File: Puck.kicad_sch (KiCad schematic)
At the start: 5 parts, among them SW1 SW_Push, SW2 SW_Push, U2 ESP32-C6-MINI-1/U

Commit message: feat: Disconnect RX and TX pins
Original-author: Ishan Karmakar <ishan.karmakar24@gmail.com>
Source-commit: 296c2ee0a068d96963a51e7bc8ff53979a0f6f0b
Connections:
- net RX: no longer names the net of U2.30 (U0RXD/GPIO17)
- net TX: no longer names the net of U2.31 (U0TXD/GPIO16)
- no-connect marks 12 -> 14
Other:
- sheet ExternalAutoprogramming (Low-Profile Female) ports: added none; removed RX, TX
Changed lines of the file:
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@@
+	)
+	(no_connect
+		(at 177.8 29.21)
 	)
 	(no_connect
@@
 	(no_connect
 		(at 121.92 57.15)
+	)
+	(no_connect
+		(at 177.8 31.75)
 	)
 	(wire
@@
 			(width 0)
 			(type default)
-		)
-	)
-	(label "TX"
-		(at 177.8 29.21 0)
-		(effects
-			(font
-				(size 1.27 1.27)
-			)
-			(justify left bottom)
 		)
 	)
@@
 		)
 	)
-	(label "RX"
-		(at 177.8 31.75 0)
-		(effects
-			(font
-				(size 1.27 1.27)
-			)
-			(justify left bottom)
-		)
-	)
 	(label "IO3"
 		(at 121.92 41.91 180)
@@
 		)
 	)
-	(label "RX"
-		(at 46.99 77.47 0)
-		(effects
-			(font
-				(size 1.27 1.27)
-			)
-			(justify left bottom)
-		)
-	)
 	(label "BOOT"
 		(at 29.21 77.47 180)
@@
 			)
 			(justify right bottom)
-		)
-	)
-	(label "TX"
-		(at 46.99 80.01 0)
-		(effects
-			(font
-				(size 1.27 1.27)
-			)
-			(justify left bottom)
 		)
 	)
@@
 			)
 		)
-		(pin "RX" bidirectional
-			(at 46.99 77.47 0)
-			(effects
-				(font
-					(size 1.27 1.27)
-				)
-				(justify right)
-			)
-		)
-		(pin "TX" bidirectional
-			(at 46.99 80.01 0)
-			(effects
-				(font
-					(size 1.27 1.27)
-				)
-				(justify right)
-			)
-		)

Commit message: feat: Remove the BOOT pin + NC GPIO9
Original-author: Ishan Karmakar <ishan.karmakar24@gmail.com>
Source-commit: 8bb5acb199ee9e43bb7b500971a5340ad49e3dfa
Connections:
- net BOOT: no longer names the net of U2.29 (GPIO23)
- net IO9: no longer names the net of U2.23 (GPIO9)
- no-connect marks 14 -> 16
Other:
- sheet ExternalAutoprogramming (Low-Profile Female) ports: added none; removed BOOT
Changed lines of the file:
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@@
+	)
+	(no_connect
+		(at 177.8 52.07)
 	)
 	(no_connect
@@
 	(no_connect
 		(at 177.8 29.21)
+	)
+	(no_connect
+		(at 177.8 72.39)
 	)
 	(no_connect
@@
 		)
 	)
-	(label "BOOT"
-		(at 177.8 72.39 0)
-		(effects
-			(font
-				(size 1.27 1.27)
-			)
-			(justify left bottom)
-		)
-	)
 	(label "IO3"
 		(at 121.92 41.91 180)
-		(effects
-			(font
-				(size 1.27 1.27)
-			)
-			(justify right bottom)
-		)
-	)
-	(label "IO9"
-		(at 177.8 52.07 0)
-		(effects
-			(font
-				(size 1.27 1.27)
-			)
-			(justify left bottom)
-		)
-	)
-	(label "BOOT"
-		(at 29.21 77.47 180)
 		(effects
 			(font
@@
 			)
 		)
-		(pin "BOOT" bidirectional
-			(at 29.21 77.47 180)
-			(effects
-				(font
-					(size 1.27 1.27)
-				)
-				(justify left)
-			)
-		)

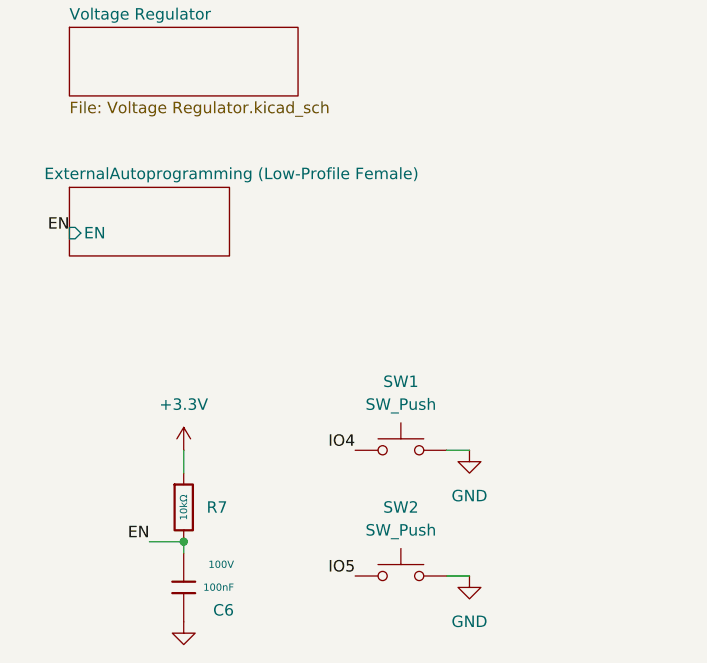
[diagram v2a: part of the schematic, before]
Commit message: feat: Remove autoprogramming sheet
Original-author: Ishan Karmakar <ishan.karmakar24@gmail.com>
Source-commit: 11d90a359a53dbe271e216bf89b8d8400085b4c9
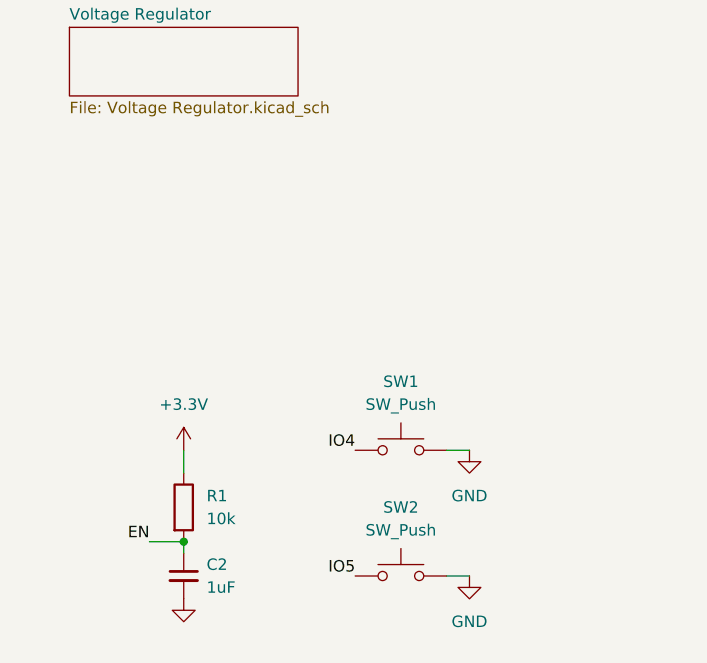
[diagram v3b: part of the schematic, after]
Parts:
- removed C6: 100nF, PCM_JLCPCB:C_0805, symbol PCM_JLCPCB-Capacitors:0805,100nF
- removed R7: 10kΩ, PCM_JLCPCB:R_0603, symbol PCM_JLCPCB-Resistors:0603,10kΩ
- added C2: 1uF, Capacitor_SMD:C_0603_1608Metric, symbol Device:C_Small
- added R1: 10k, Resistor_SMD:R_0603_1608Metric, symbol Device:R
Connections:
- net +3.3V: now also R1.1
- net EN: now also C2.1, R1.2
- net GND: now also C2.2
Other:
- removed sheet ExternalAutoprogramming (Low-Profile Female)

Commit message: feat: Wire D+ and D- from Type C recepticle to ESP32 pins
Original-author: Ishan Karmakar <ishan.karmakar24@gmail.com>
Source-commit: f485fb4ecb58e7db9c11b8a83e3a2328aeb9ad39
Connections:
- net D-: now reaches U2.17 (GPIO12/USB_D-)
- net D+: now reaches U2.18 (GPIO13/USB_D+)
- no-connect marks 16 -> 14
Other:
- sheet Type C Recepticle (No Flash) renamed Type C Recepticle
- sheet Type C Recepticle ports: added D+, D-; removed none
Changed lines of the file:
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@@
-	)
-	(no_connect
-		(at 177.8 36.83)
 	)
 	(no_connect
 		(at 121.92 34.29)
-	)
-	(no_connect
-		(at 177.8 39.37)
 	)
 	(no_connect
@@
 		)
 	)
+	(label "D+"
+		(at 177.8 36.83 0)
+		(effects
+			(font
+				(size 1.27 1.27)
+			)
+			(justify left bottom)
+		)
+	)
 	(label "IO3"
 		(at 121.92 41.91 180)
@@
 		)
 	)
+	(label "D-"
+		(at 54.61 29.21 0)
+		(effects
+			(font
+				(size 1.27 1.27)
+			)
+			(justify left bottom)
+		)
+	)
 	(label "IO3"
 		(at 95.25 26.67 0)
@@
 		)
 	)
+	(label "D-"
+		(at 177.8 39.37 0)
+		(effects
+			(font
+				(size 1.27 1.27)
+			)
+			(justify left bottom)
+		)
+	)
 	(label "IO19"
 		(at 177.8 62.23 0)
@@
 			)
 			(justify right bottom)
+		)
+	)
+	(label "D+"
+		(at 54.61 25.4 0)
+		(effects
+			(font
+				(size 1.27 1.27)
+			)
+			(justify left bottom)
 		)
 	)
@@
 			(color 255 255 194 1)
 		)
-		(property "Sheetname" "Type C Recepticle (No Flash)"
+		(property "Sheetname" "Type C Recepticle"
 			(at 29.21 23.4184 0)
 			(show_name no)
@@
 			)
 		)
+		(pin "D+" input
+			(at 54.61 25.4 0)
+			(effects
+				(font
+					(size 1.27 1.27)
+				)
+				(justify right)
+			)
+		)
+		(pin "D-" input
+			(at 54.61 29.21 0)
+			(effects
+				(font
+					(size 1.27 1.27)
+				)
+				(justify right)
+			)
+		)
